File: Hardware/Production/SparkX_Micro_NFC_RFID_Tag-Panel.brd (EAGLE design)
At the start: 156.7 x 77.7 mm, 586 parts, among them J1 QWIIC_RIGHT_ANGLE, J10 QWIIC_RIGHT_ANGLE, J11 QWIIC_RIGHT_ANGLE, J12 QWIIC_RIGHT_ANGLE, J13 QWIIC_RIGHT_ANGLE, J14 QWIIC_RIGHT_ANGLE, J15 QWIIC_RIGHT_ANGLE, J16 QWIIC_RIGHT_ANGLE, J17 QWIIC_RIGHT_ANGLE, J18 QWIIC_RIGHT_ANGLE, J19 QWIIC_RIGHT_ANGLE, J2 QWIIC_RIGHT_ANGLE, J20 QWIIC_RIGHT_ANGLE, J3 QWIIC_RIGHT_ANGLE, J4 QWIIC_RIGHT_ANGLE, J5 QWIIC_RIGHT_ANGLE, J6 QWIIC_RIGHT_ANGLE, J7 QWIIC_RIGHT_ANGLE, J8 QWIIC_RIGHT_ANGLE, J9 QWIIC_RIGHT_ANGLE, U1 ST25DV64KC, U10 ST25DV64KC, U11 ST25DV64KC, U12 ST25DV64KC, U13 ST25DV64KC, U14 ST25DV64KC, U15 ST25DV64KC, U16 ST25DV64KC, U17 ST25DV64KC, U18 ST25DV64KC, U19 ST25DV64KC, U2 ST25DV64KC, U20 ST25DV64KC, U3 ST25DV64KC, U4 ST25DV64KC, U5 ST25DV64KC, U6 ST25DV64KC, U7 ST25DV64KC, U8 ST25DV64KC, U9 ST25DV64KC

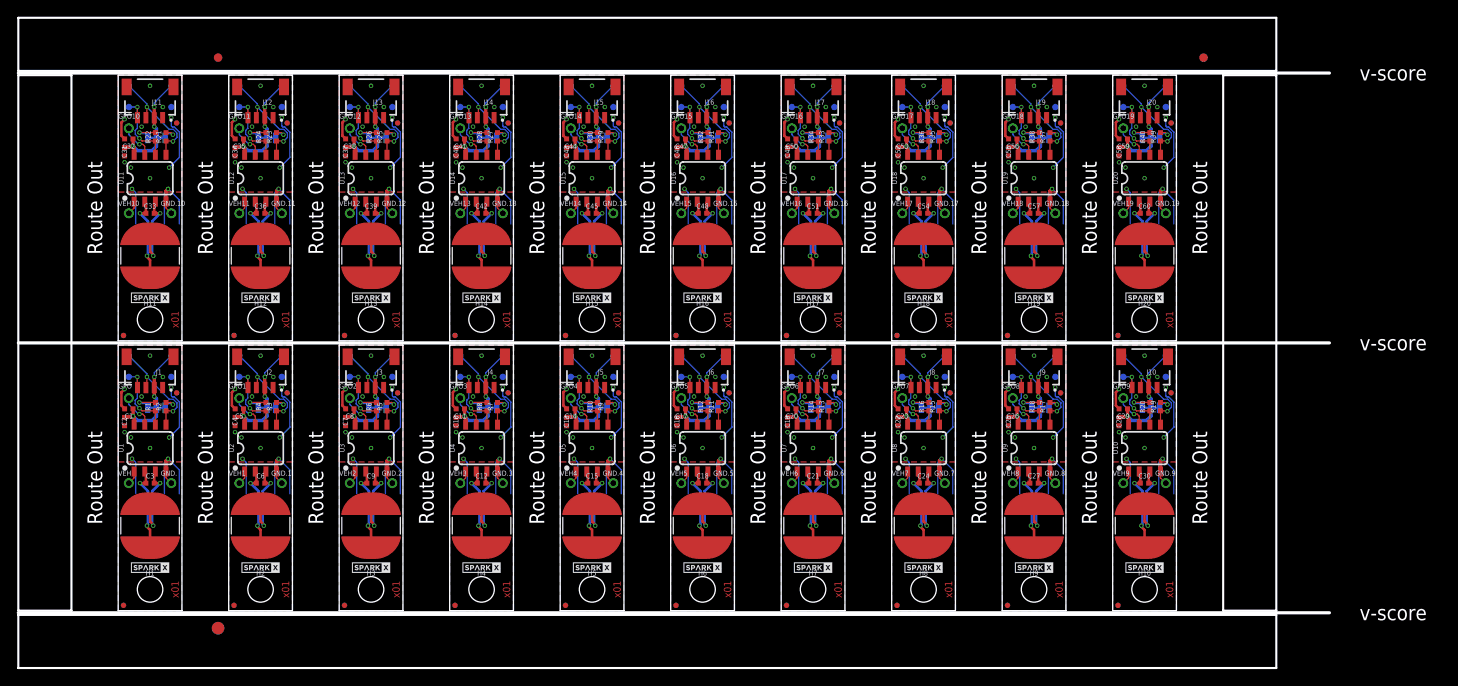
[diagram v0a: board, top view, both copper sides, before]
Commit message: Remove GND from under antenna
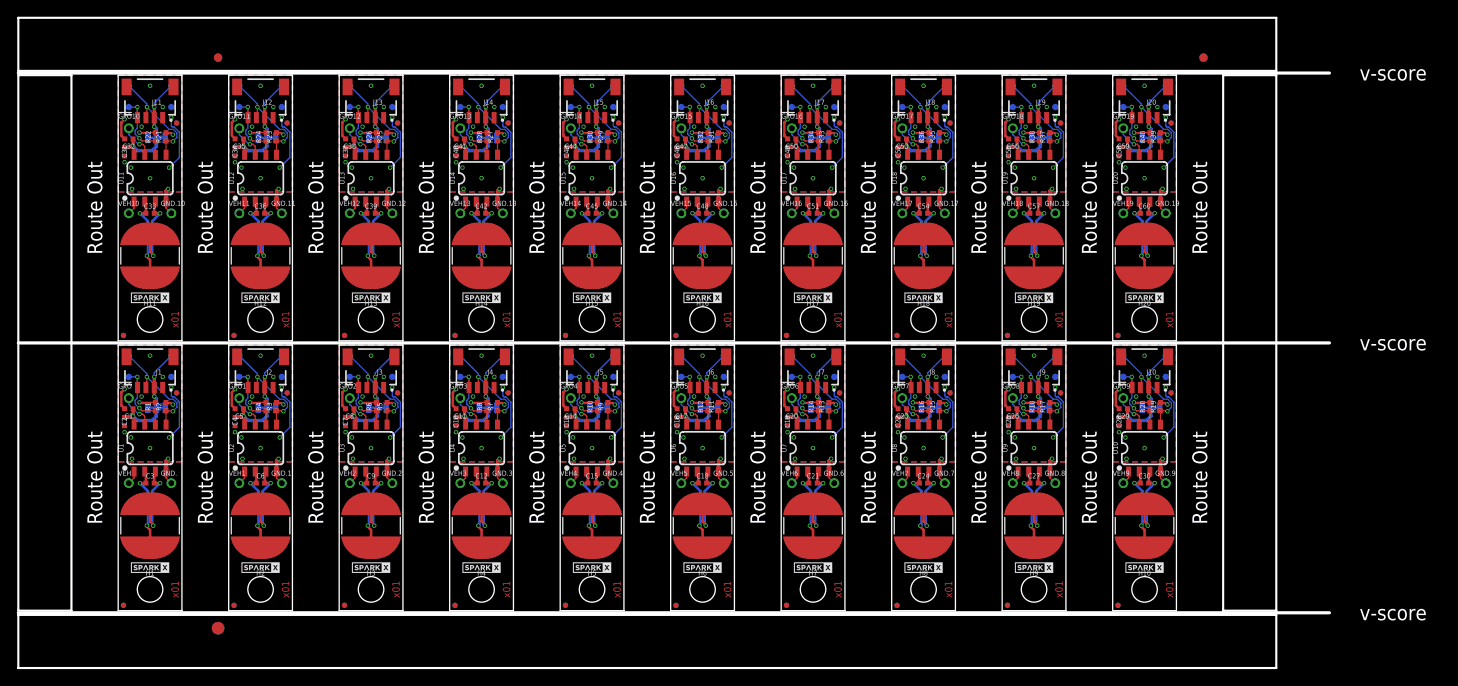
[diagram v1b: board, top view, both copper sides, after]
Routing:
- net GND4: track 26.5 -> 13.0 mm
- net GND6: track 26.5 -> 13.0 mm
- net GND7: track 26.5 -> 13.0 mm
- net GND: track 26.5 -> 13.0 mm
- net GND5: track 26.5 -> 13.0 mm
- net GND1: track 26.5 -> 13.0 mm
- net GND9: track 26.5 -> 13.0 mm
- net GND8: track 26.5 -> 13.0 mm
- net GND14: track 26.5 -> 13.0 mm
- net GND2: track 26.5 -> 13.0 mm
- net GND16: track 26.5 -> 13.0 mm
- net GND3: track 26.5 -> 13.0 mm
- net GND12: track 26.5 -> 13.0 mm
- net GND15: track 26.5 -> 13.0 mm
- net GND11: track 26.5 -> 13.0 mm
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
